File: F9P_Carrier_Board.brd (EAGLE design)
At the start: 5 x 8.6 mm, 53 parts, among them J2 JTAG, J6 MICROMOD-2222-C, U5 AP7361C-33

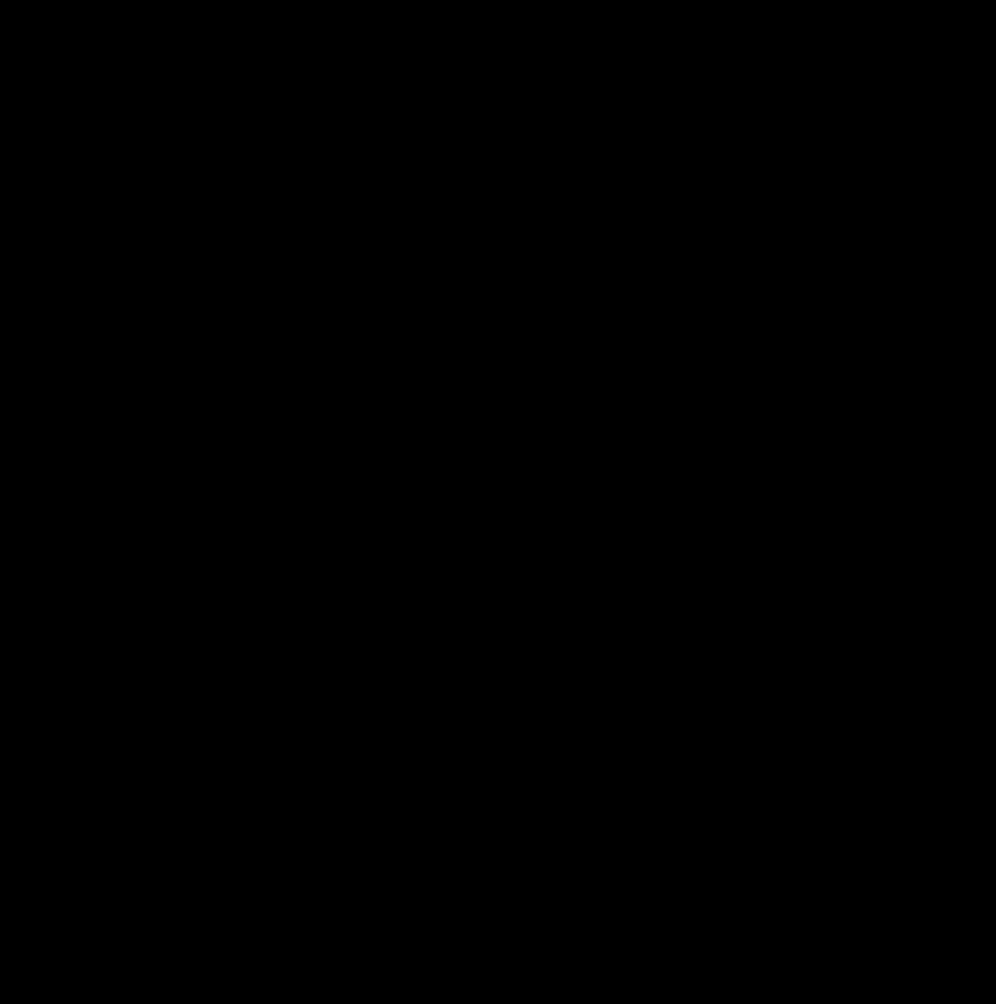
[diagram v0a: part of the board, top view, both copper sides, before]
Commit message: Adds the F9R and the ESD protection diode
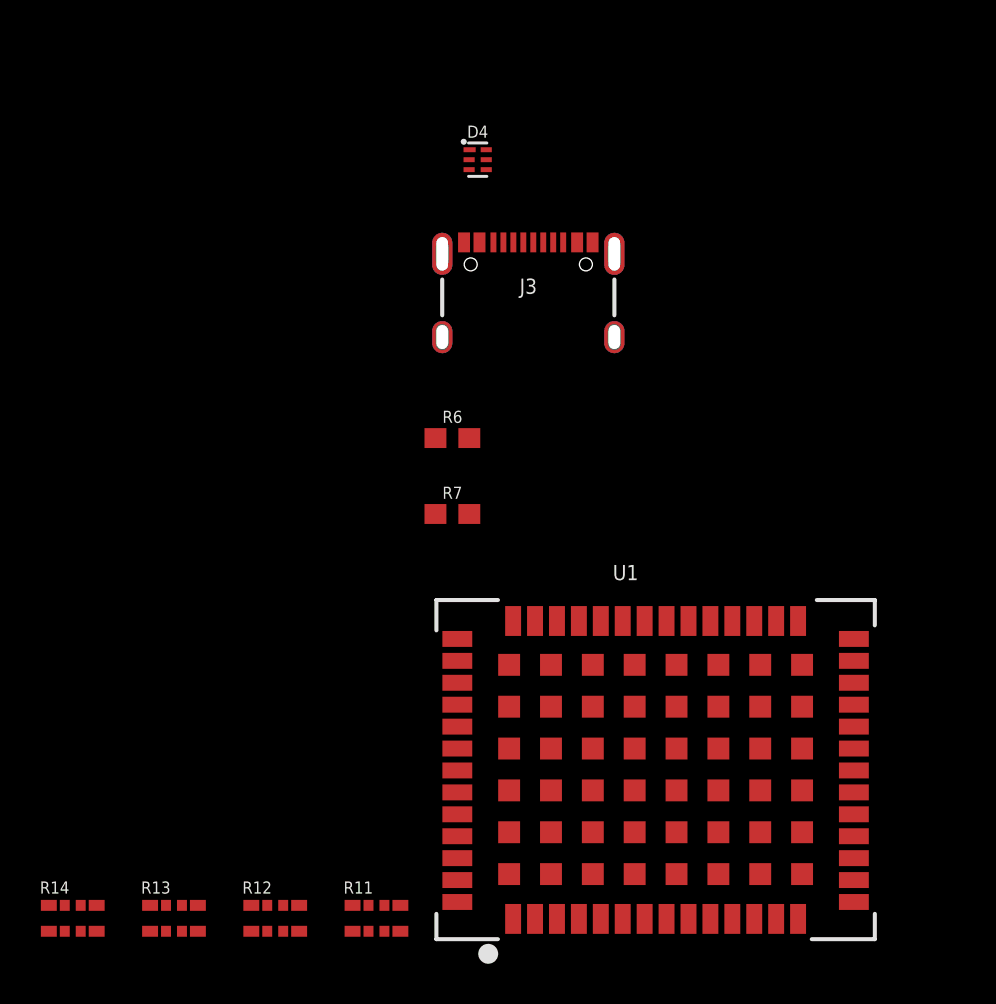
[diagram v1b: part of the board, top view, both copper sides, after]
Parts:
- added D4: PRTR5V0U2F, SparkFun-IC-Power:SOT886
- added J3: (no value), SparkFun-Connectors:USB-C-16P-2LAYER-PADS
- added R11, R12, R13, R14: 33, SparkFun-Resistors:1206_RA
- added R6, R7: 5.1k, SparkFun-Resistors:0603
- added U1: U-BLOX_ZED_F9R, SparkFun-GPS:UBLOX_ZED_F9R
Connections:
- new net N$12: D4.1, J3.A6, J3.B6
- new net N$13: D4.3, J3.A7, J3.B7
- new net N$15: R11.P2, U1.P49
- new net N$16: R11.P4, U1.P51
- new net N$17: D4.6
- new net N$18: D4.4
- new net N$19: R11.P1, U1.P46
- new net N$20: R11.P3, U1.P50
- new net N$21: R12.P3, U1.P44
- new net N$22: R12.P4, U1.P45
- new net N$23: R12.P1, U1.P42
- new net N$24: R12.P2, U1.P43
- new net N$25: R13.P1, U1.P27
- new net N$26: R13.P2, U1.P26
- new net N$27: R13.P5, U1.P23
- new net N$28: R13.P6, U1.P22
- new net N$29: R14.P1, U1.P19
- new net N$30: R14.P2, U1.P20
- new net N$31: U1.P33, U1.P34
- new net N$6: D4.2, J3.A5, R6.2
- new net N$7: J3.B5, R7.2
- new net N$8: J3.VBUS1, J3.VBUS2
- new net N$9: D4.5
- new net V_BKCP: U1.P36
- net GND: now also J3.GND, J3.GND2, R6.1, R7.1, U1.G1, U1.G10, U1.G11, U1.G12, U1.G13, U1.G14, U1.G15, U1.G16, U1.G17, U1.G18, U1.G19, U1.G2, U1.G20, U1.G21, U1.G22, U1.G23, U1.G24, U1.G25, U1.G26, U1.G27, U1.G28, U1.G29, U1.G3, U1.G30, U1.G31, U1.G32, U1.G33, U1.G34, U1.G35, U1.G36, U1.G37, U1.G38, U1.G39, U1.G4, U1.G40, U1.G41, U1.G42, U1.G43, U1.G44, U1.G45, U1.G46, U1.G47, U1.G48, U1.G5, U1.G6, U1.G7, U1.G8, U1.G9, U1.P1, U1.P12, U1.P14, U1.P3, U1.P32, U1.P37, U1.P41, U1.P48
- net V_USB: now also U1.P38

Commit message: Mostly finishes schematic
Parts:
- removed 3V3_LED, VIN_LED: JUMPER-SMT_2_NC_TRACE_SILK, SparkFun-Jumpers:SMT-JUMPER_2_NC_TRACE_SILK
- removed J2: JTAG, SparkFun-Connectors:2X5-PTH-1.27MM
- added 3V3, GEOF, PPS, RTK, VIN: JUMPER-SMT_2_NC_TRACE_SILK, SparkFun-Jumpers:SMT-JUMPER_2_NC_TRACE_SILK
- added BT2: ML414H_IV01E_BATTERY, SparkFun-Batteries:ML414H_IV01E
- added C3, C4: 0.1uF, SparkFun-Capacitors:0402-TIGHT
- added C8: 47pF, SparkFun-Capacitors:0402
- added D10, D8, D9: BLUE, SparkFun-LED:LED-0603
- added D11: 0.5A/40V/420mV, SparkFun-DiscreteSemi:SOD-323
- added FB1: FERRITE_BEAD-120_OHM-0402T, SparkFun-Coils:0402-TIGHT
- added FD2, FD4: FIDUCIALUFIDUCIAL, SparkFun-Aesthetics:FIDUCIAL-MICRO
- added H1, H2, H3, H4: STAND-OFFTIGHT, SparkFun-Hardware:STAND-OFF-TIGHT
- added J10: (no value), SparkFun-Connectors:1X09_NO_SILK
- added J4: U.FL, SparkFun-Connectors:U.FL
- added J5: QWIIC_RIGHT_ANGLE, SparkFun-Connectors:JST04_1MM_RA
- added J7: (no value), SparkFun-Connectors:1X08_NO_SILK
- added J8: JTAG, SparkFun-Connectors:2X5-PTH-1.27MM
- added J9: (no value), SparkFun-Connectors:1X06_NO_SILK
- added JP5: JUMPER-SMT_2_NO_SILK, SparkFun-Jumpers:SMT-JUMPER_2_NO_SILK
- added LOGO1: SFE_LOGO_NAME.1_INCH, SparkFun-Aesthetics:SFE_LOGO_NAME_.1
- added R15, R16: 27OHM, SparkFun-Resistors:0402-TIGHT
- added R17: 33, SparkFun-Resistors:0603
- added R19, R20, R21: 1KOHM-0402-1/16W-1%, SparkFun-Resistors:0402
- added R22: 100k, SparkFun-Resistors:0402-TIGHT
- added R24: 3.3k, SparkFun-Resistors:0603
- U1: value U-BLOX_ZED_F9R -> U-BLOX_ZED-F9P; device SparkFun-GPS:UBLOX_ZED_F9R -> SparkFun-GPS:ZED-F9P
- moved R13 230.5 mm to (121.9, 121.9), turned to 90 degrees
- moved R14 230.0 mm to (123.2, 115.6), turned to 90 degrees
- moved R12 134.6 mm to (81.0, 32.0), turned to 270 degrees
- moved R11 128.0 mm to (81.3, 27.4), turned to 270 degrees
- moved U1 123.1 mm to (95.5, 26.6)
- moved D4 108.4 mm to (30.0, 85.1)
- moved J3 88.7 mm to (13.5, 67.3)
- moved R6 88.7 mm to (9.65, 57.1)
- moved R7 88.7 mm to (9.65, 53.3)
- moved BYP 8.92 mm to (12.2, 36.6)
- moved U$51 8.92 mm to (18.8, 35.5)
- moved BT1 8.92 mm to (70.4, 46.7)
- moved D2 8.92 mm to (7.37, 17.8)
- moved D3 8.92 mm to (7.37, 15.7)
- moved D6 8.92 mm to (65.3, 47.8)
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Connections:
- net SCL renamed SCL/SCK
- removed net !CS!: J6.55
- removed net !CS1!/DAT3: J6.70
- removed net !RESET: J2.10, J6.6, S1.3, S1.4
- removed net A0: J6.34
- removed net A1: J6.38
- removed net CAN_RXI: J6.41
- removed net CAN_TXO: J6.43
- removed net CIPO: J6.61
- removed net CIPO1/DAT0: J6.64
- removed net COPI: J6.59
- removed net COPI1: J6.62
- removed net CTS1: J6.15
- removed net D0: J6.10
- removed net D1: J6.18
- removed net DAT1: J6.66
- removed net DAT2: J6.68
- removed net G0: J6.40
- removed net G1: J6.42
- removed net G10/ADC_P: J6.63
- removed net G11: J6.8
- removed net G2: J6.44
- removed net G3: J6.46
- removed net G4: J6.48
- removed net G5: J6.73
- removed net G6: J6.71
- removed net G7: J6.69
- removed net G8: J6.67
- removed net G9/ADC_N: J6.65
- removed net I2S_CLK: J6.50
- removed net I2S_SDI: J6.54
- removed net I2S_SDO: J6.56
- removed net I2S_WS: J6.52
- removed net MCLK: J6.58
- removed net N$31: U1.P33, U1.P34
- removed net PWM0: J6.32
- removed net PWM1: J6.47
- removed net RTS1: J6.13
- removed net RX1: J6.19
- removed net RX2: J6.20
- removed net SCK: J6.57
- removed net SCK1: J6.60
- removed net SCL1: J6.53
- removed net SDA: J6.12
- removed net SDA1: J6.51
- removed net TX1: J6.17
- removed net TX2: J6.22
- removed net USBHOST_N: J6.37
- removed net USBHOST_P: J6.35
- removed net V_BKCP: U1.P36
- new net !RESET!: J6.6, J8.10, S1.3, S1.4
- new net !SAFEBOOT: J10.3
- new net !SAFEBOOT!: R11.P6
- new net !ZED_RESET!: J10.4, R11.P7
- new net D_SEL: JP5.1, U1.47
- new net GEOF_STAT: D10.A
- new net GEO_STAT: U1.19
- new net INT: J10.2, R11.P5
- new net N$32: D11.C, R24.2
- new net N$45: GEOF.2, R21.1
- new net N$46: D10.C, R21.2
- new net PPS: D8.A, J10.1, U1.53
- new net RF_IN: FB1.1, J4.FEED, U1.2
- new net RTK_STAT: D9.A, R14.P7
- new net RXI/SDI: J6.17, J6.61, J7.5, R12.P7
- new net RXI2: J6.22, J9.4, R13.P7
- new net SCL/CLK: J10.6, J5.4, J6.57, J7.7, R12.P5
- new net SDA/!CS!: J10.7, J5.3, J6.12, J6.55, J7.4, R12.P6
- new net TXO/SDO: J6.19, J6.59, J7.6, R12.P8
- new net TXO2: J6.20, J9.5, R13.P8
- new net TX_READY: J10.5, R11.P8
- new net V_BATT: BT2.+, R24.1, U1.36
- new net V_RF: R17.2, U1.7
- new net ZED_USB_N: R16.2, U1.39
- new net ZED_USB_P: R15.2, U1.40
- net 3.3V: now also C3.1, C4.1, D11.A, D2.A, J10.8, J5.2, J7.3, J8.1, R22.2, U1.33, U1.34, U1.38; no longer J2.1, R1.2
- net GND: now also 3V3.2, BT2.-, C3.2, C4.2, C8.2, GEOF.1, J10.9, J4.1, J4.2, J5.1, J7.1, J7.8, J8.3, J8.5, J8.9, J9.1, JP5.2, PPS.1, R22.1, RTK.1, U1.1, U1.100, U1.101, U1.102, U1.12, U1.14, U1.3, U1.32, U1.37, U1.41, U1.48, U1.55, U1.56, U1.57, U1.58, U1.59, U1.60, U1.61, U1.62, U1.63, U1.64, U1.65, U1.66, U1.67, U1.68, U1.69, U1.70, U1.71, U1.72, U1.73, U1.74, U1.75, U1.76, U1.77, U1.78, U1.79, U1.80, U1.81, U1.82, U1.83, U1.84, U1.85, U1.86, U1.87, U1.88, U1.89, U1.90, U1.91, U1.92, U1.93, U1.94, U1.95, U1.96, U1.97, U1.98, U1.99, VIN.2; no longer 3V3_LED.2, J2.3, J2.5, J2.9, U1.G1, U1.G10, U1.G11, U1.G12, U1.G13, U1.G14, U1.G15, U1.G16, U1.G17, U1.G18, U1.G19, U1.G2, U1.G20, U1.G21, U1.G22, U1.G23, U1.G24, U1.G25, U1.G26, U1.G27, U1.G28, U1.G29, U1.G3, U1.G30, U1.G31, U1.G32, U1.G33, U1.G34, U1.G35, U1.G36, U1.G37, U1.G38, U1.G39, U1.G4, U1.G40, U1.G41, U1.G42, U1.G43, U1.G44, U1.G45, U1.G46, U1.G47, U1.G48, U1.G5, U1.G6, U1.G7, U1.G8, U1.G9, U1.P1, U1.P12, U1.P14, U1.P3, U1.P32, U1.P37, U1.P41, U1.P48, VIN_LED.2
- net N$1: now also D2.C, R1.2; no longer D2.A, R1.1
- net N$15: now also U1.49; no longer U1.P49
- net N$16: now also U1.51; no longer U1.P51
- net N$17: now also D4.4, R16.1; no longer D4.6
- net N$18: now also C8.1, FB1.2, R17.1; no longer D4.4
- net N$19: now also U1.46; no longer U1.P46
- net N$2: now also VIN.1; no longer D3.A
- net N$20: now also U1.50; no longer U1.P50
- net N$21: now also U1.44; no longer U1.P44
- net N$22: now also U1.45; no longer U1.P45
- net N$23: now also U1.42; no longer U1.P42
- net N$24: now also U1.43; no longer U1.P43
- net N$25: now also U1.27; no longer U1.P27
- net N$26: now also U1.26; no longer U1.P26
- net N$27: now also PPS.2, R19.1; no longer R13.P5, U1.P23
- net N$28: now also D8.C, R19.2; no longer R13.P6, U1.P22
- net N$29: now also D9.C, R20.2; no longer R14.P1, U1.P19
- net N$3: now also 3V3.1, R1.1; no longer 3V3_LED.1, D2.C
- net N$30: now also U1.20; no longer U1.P20
- net N$4: now also R4.2; no longer VIN_LED.1
- net N$8: now also R20.1, RTK.2; no longer J3.VBUS1, J3.VBUS2
- net N$9: now also D4.6, R15.1; no longer D4.5
- net SWDCK: now also J8.4; no longer J2.4
- net SWDIO: now also J8.2; no longer J2.2
- net VIN: now also D3.A, D4.5, J1.VBUS1, J1.VBUS2, J3.VBUS1, J3.VBUS2, J7.2; no longer R4.2
- net V_USB: no longer J1.VBUS1, J1.VBUS2, U1.P38
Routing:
- net !RESET: track 50.2 -> 0.00 mm, vias 3 -> 0
- net !RESET!: track 0.00 -> 5.59 mm
- net RXI/SDI: track 0.00 -> 4.09 mm
- net I2S_SDO: track 4.06 -> 0.00 mm
- net TXO/SDO: track 0.00 -> 4.03 mm
- net SDA/!CS!: track 0.00 -> 4.02 mm
- net SWDCK: track 12.6 -> 8.60 mm
- net I2S_SDI: track 3.98 -> 0.00 mm
- net MCLK: track 3.82 -> 0.00 mm
- net I2S_WS: track 3.78 -> 0.00 mm
- net I2S_CLK: track 3.66 -> 0.00 mm
- net SCK1: track 3.30 -> 0.00 mm
- net A1: track 3.06 -> 0.00 mm
- net G0: track 2.95 -> 0.00 mm
- net G1: track 2.82 -> 0.00 mm
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
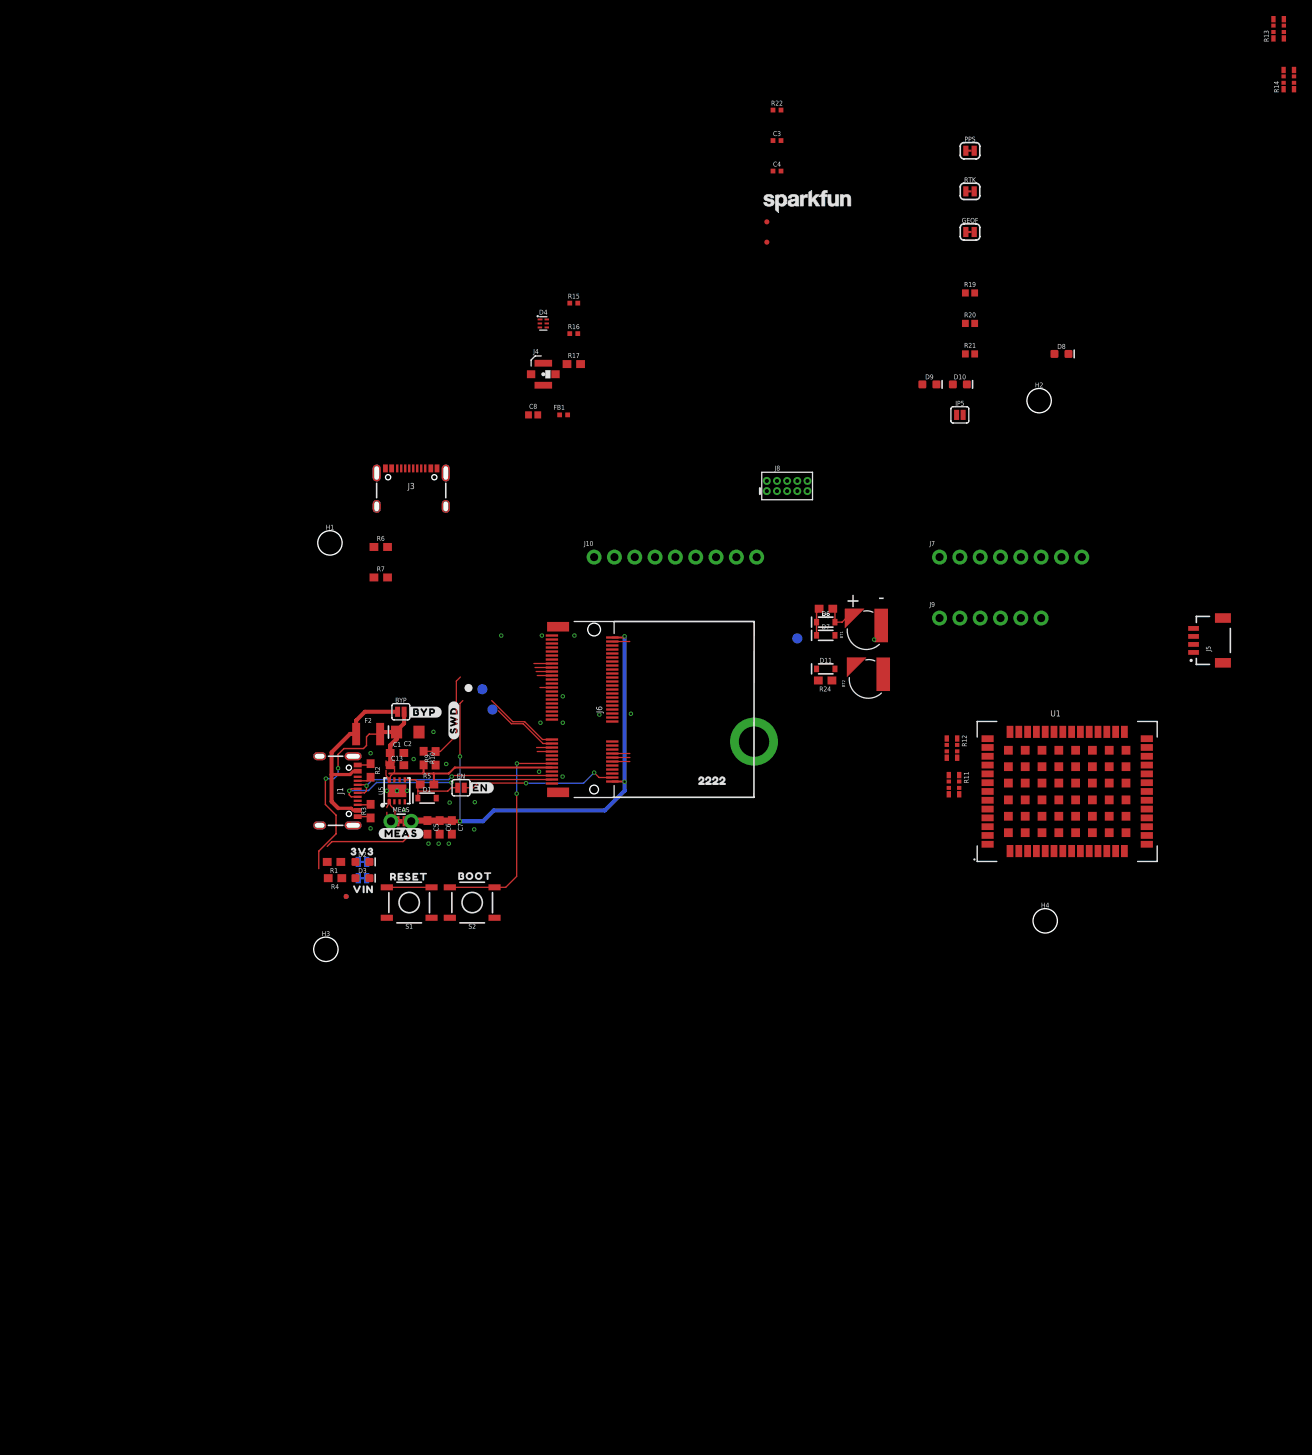
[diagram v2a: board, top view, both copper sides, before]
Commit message: Puts parts generally where they will be routed
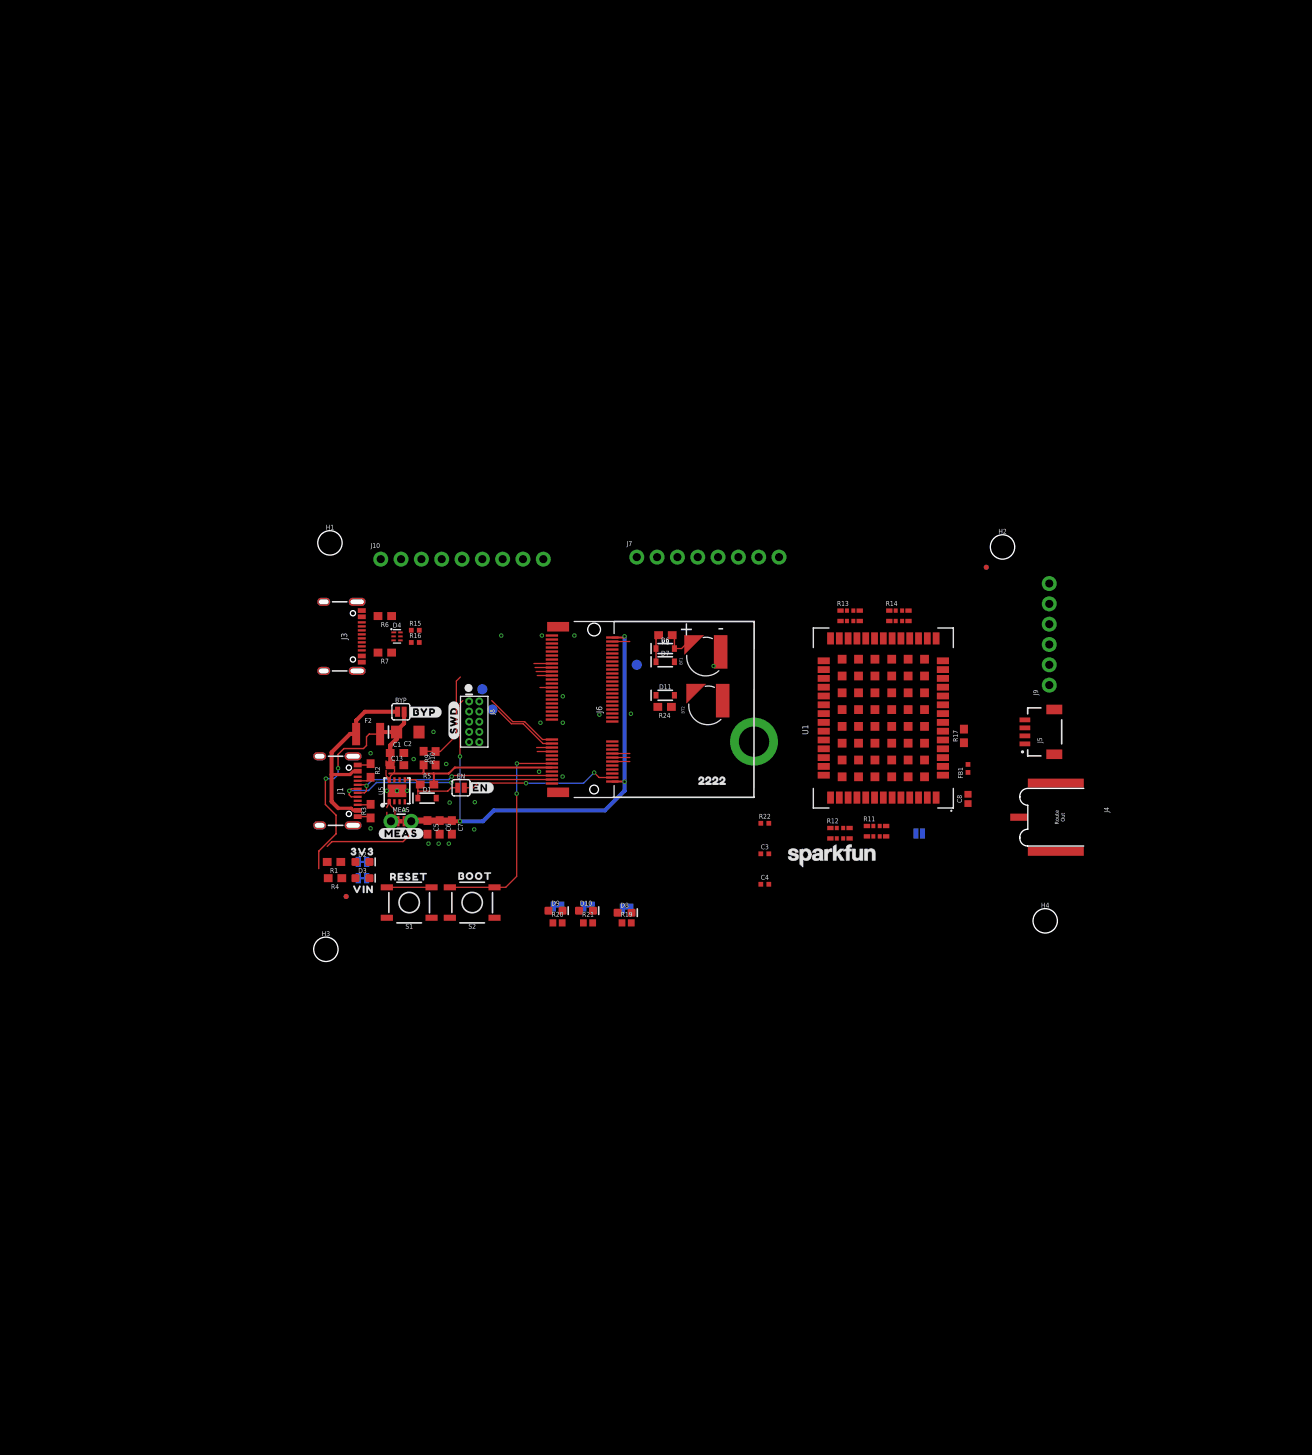
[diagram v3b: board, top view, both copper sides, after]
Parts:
- J4: device SparkFun-Connectors:U.FL -> SparkFun-RF:SMA-EDGE-SMD
- moved PPS 104.0 mm to (40.4, 11.9), flipped to the bottom
- moved RTK 103.2 mm to (31.8, 12.2), flipped to the bottom
- moved GEOF 96.9 mm to (35.6, 12.2), flipped to the bottom
- moved R20 91.0 mm to (31.8, 10.2)
- moved R13 90.9 mm to (68.3, 48.5), turned to 0 degrees
- moved R19 89.7 mm to (40.4, 10.2)
- moved C3 89.2 mm to (57.7, 18.8)
- moved C4 89.2 mm to (57.7, 15.0)
- moved R22 89.2 mm to (57.7, 22.6)
- moved D8 88.7 mm to (40.1, 11.4)
- moved J4 87.4 mm to (97.5, 23.4), turned to 270 degrees
- moved R21 85.7 mm to (35.6, 10.2)
- moved R14 82.9 mm to (74.4, 48.5), turned to 0 degrees
- moved LOGO1 81.8 mm to (66.0, 18.5)
- moved D10 80.7 mm to (35.3, 11.7)
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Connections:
- net GND: now also J4.GND@0, J4.GND@1; no longer J4.1, J4.2
- net RF_IN: now also J4.SIG; no longer J4.FEED
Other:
- board size 5 x 8.6 mm -> 8 x 7.2 mm

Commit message: Still situating the parts within the  board
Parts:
- removed J7: (no value), SparkFun-Connectors:1X08_NO_SILK
- removed R14: 33, SparkFun-Resistors:1206_RA
- J10: device SparkFun-Connectors:1X09_NO_SILK -> SparkFun-Connectors:1X12_NO_SILK_KIT
- moved J10 59.1 mm to (35.1, 2.29)
- moved R20 44.9 mm to (64.8, 40.6)
- moved R21 44.9 mm to (68.6, 40.6)
- moved R19 44.0 mm to (72.1, 40.6)
- moved D9 42.6 mm to (64.5, 38.6)
- moved D10 42.6 mm to (68.3, 38.6)
- moved GEOF 42.4 mm to (68.6, 38.7)
- moved RTK 42.4 mm to (64.8, 38.7)
- moved D8 41.8 mm to (71.9, 38.6)
- moved PPS 41.5 mm to (72.1, 38.7)
- moved LOGO1 32.1 mm to (39.1, 36.1)
- moved J5 30.7 mm to (78.9, 5.46), turned to 0 degrees
- moved U$55 20.5 mm to (38.2, 10.2)
- moved TP1 20.4 mm to (40.4, 22.1)
- moved BT2 19.5 mm to (46.6, 18.3)
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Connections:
- removed net N$30: R14.P2, U1.20
- net 3.3V: now also J10.9, J9.3; no longer J10.8, J7.3
- net GND: now also J10.10; no longer J10.9, J7.1, J7.8
- net N$15: now also R11.P1, U1.51; no longer R11.P2, U1.49
- net N$16: now also R11.P2, U1.50; no longer R11.P4, U1.51
- net N$19: now also R11.P3, U1.49; no longer R11.P1, U1.46
- net N$20: now also R11.P4, U1.46; no longer R11.P3, U1.50
- net N$21: now also R12.P1, U1.45; no longer R12.P3, U1.44
- net N$22: now also R12.P2, U1.44; no longer R12.P4, U1.45
- net N$23: now also R12.P3, U1.43; no longer R12.P1, U1.42
- net N$24: now also R12.P4, U1.42; no longer R12.P2, U1.43
- net RTK_STAT: now also U1.20; no longer R14.P7
- net RXI/SDI: now also J10.11; no longer J7.5
- net SCL/CLK: now also J10.7; no longer J10.6, J7.7
- net SDA/!CS!: now also J10.8; no longer J10.7, J7.4
- net TXO/SDO: now also J10.12; no longer J7.6
- net VIN: now also J10.6; no longer J7.2
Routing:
- net N$5: track 19.6 -> 3.64 mm, vias 2 -> 1
- net !BOOT!: track 27.4 -> 12.4 mm, vias 2 -> 1
- net VIN/3: track 13.9 -> 3.60 mm
- net VIN: track 56.6 -> 48.2 mm
- net SWDIO: track 10.2 -> 4.71 mm
- net SWDCK: track 8.60 -> 4.26 mm
- net 3.3V: track 79.5 -> 76.4 mm
- net SCL/SCK: track 2.20 -> 0.00 mm
- net I2C_!INT: track 2.20 -> 0.00 mm
- net SDA/!CS!: track 4.02 -> 1.83 mm
- net TXO/SDO: track 4.03 -> 2.11 mm
- net RXI/SDI: track 4.09 -> 2.25 mm
- net USB_P: track 28.7 -> 30.2 mm
- net RTC_3V: track 5.69 -> 6.44 mm
- net GND: track 3.36 -> 2.85 mm, vias 26 -> 25
- added copper zone on layer 1, net GND
- added copper zone on layer 16, net GND
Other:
- board size 8 x 7.2 mm -> 88.9 x 41.9 mm
